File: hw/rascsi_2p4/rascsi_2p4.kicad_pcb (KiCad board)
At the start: 2 copper layers, 65 x 56 mm, 126 parts, among them J1 Raspberry_Pi_2_3, J10 Conn_01x04_Male, J2 DNP, J20 171826-4, J3 Conn_02x25_Odd_Even, J4 I2C Pinout, J5 DNP, J6 CONNFLY DB-25, J7 DNP, J8 USB_B_Micro, J9 Conn_02x25_Odd_Even, U1 74ALVC164245DGG, U2 74ALVC164245DGG, X1 Mac, X3 Mac, X7 Pi, X8 Pi

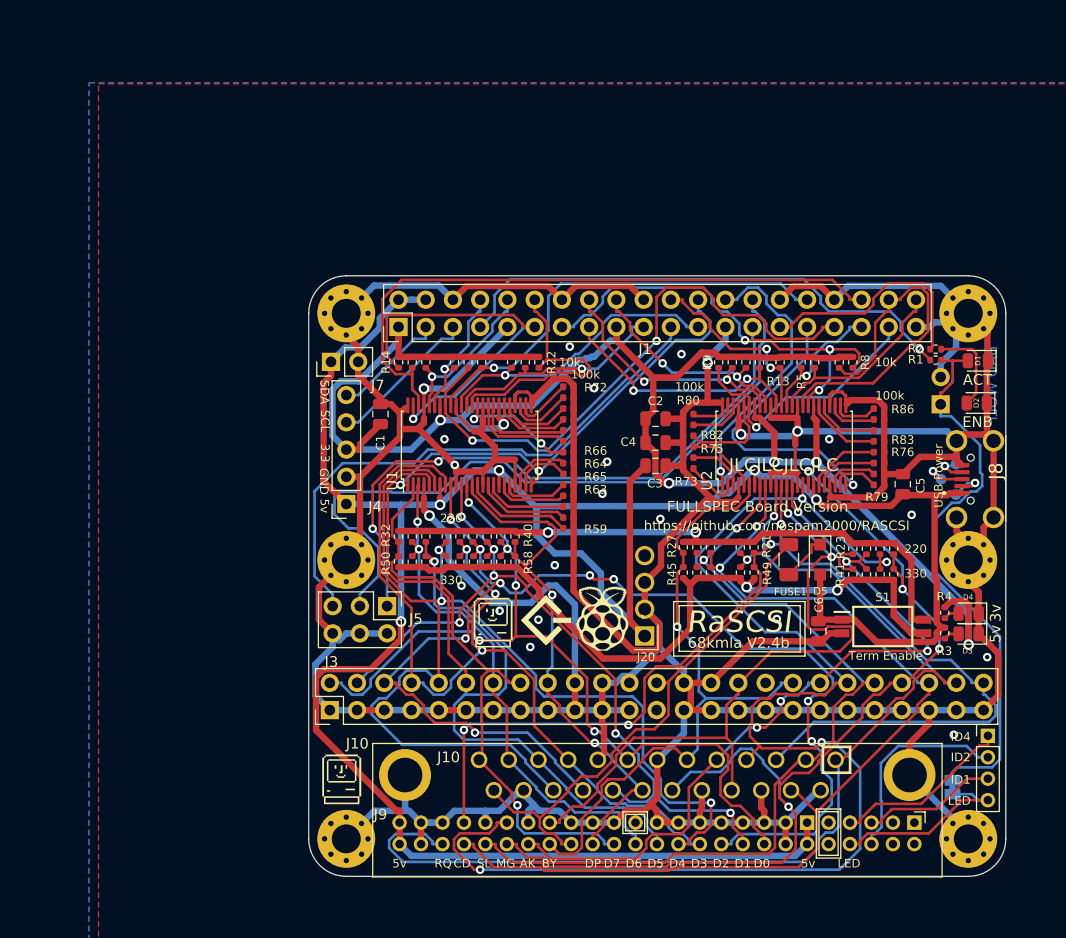
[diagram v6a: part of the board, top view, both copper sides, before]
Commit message: use active SCSI termination
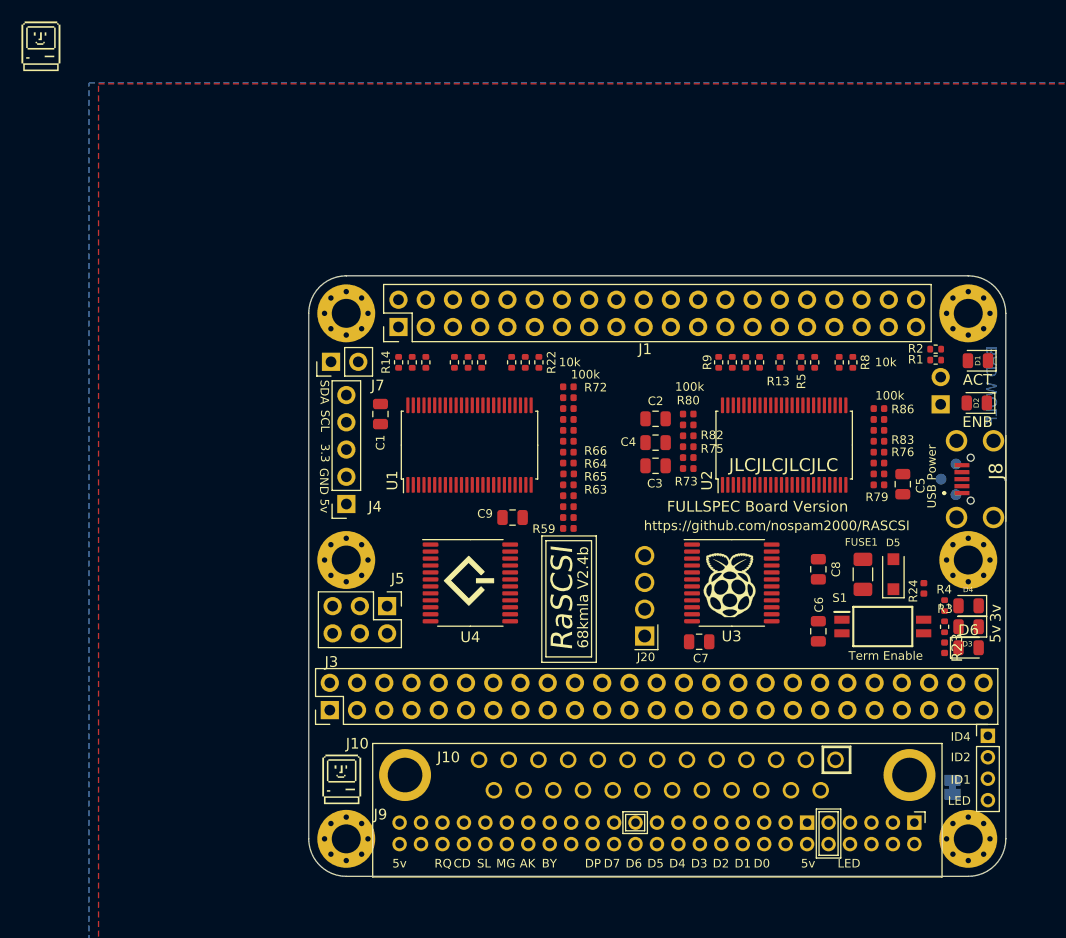
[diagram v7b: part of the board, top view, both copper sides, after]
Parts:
- removed R25, R26, R27, R28, R29, R30, R31, R32, R33, R34, R35, R36, R37, R38, R39, R40: 220, Resistor_SMD:R_0402_1005Metric
- removed R41, R42, R43, R44, R45, R46, R47, R48, R49, R50, R51, R52, R53, R54, R55, R56, R57, R58: 330, Resistor_SMD:R_0402_1005Metric
- added C7: 4u7, Capacitor_SMD:C_0805_2012Metric, F.Cu at (210.9, 76.6)
- added C8: 4u7, Capacitor_SMD:C_0805_2012Metric, F.Cu at (222.0, 69.9)
- added C9: 4u7, Capacitor_SMD:C_0805_2012Metric, F.Cu at (193.5, 65.0)
- added D6: Green, LED_SMD:LED_0805_2012Metric, F.Cu at (236.0, 77.2)
- added U3: UCC5606PWPTR, Package_SO:TSSOP-24_6.1x7.8mm_P0.65mm, F.Cu at (214.0, 71.1)
- added U4: UCC5606PWPTR, Package_SO:TSSOP-24_6.1x7.8mm_P0.65mm, F.Cu at (189.6, 71.1)
- R23: value 220 -> 2k
- R24: value 220 -> 10k
- moved X3 68.3 mm to (149.6, 21.1)
- moved R23 12.6 mm to (233.8, 77.2)
- moved X7 12.3 mm to (213.8, 71.4)
- moved X8 8.09 mm to (189.3, 70.9)
- moved FUSE1 7.04 mm to (226.2, 70.3), turned to 270 degrees
- moved D5 6.96 mm to (229.0, 70.3), turned to 90 degrees
- moved R24 6.51 mm to (231.9, 71.6), turned to 90 degrees
- moved D4 0.71 mm to (236.0, 73.3)
- moved R4 0.66 mm to (233.8, 73.3)
- moved D3 0.66 mm to (236.0, 75.2)
- moved R3 0.59 mm to (233.8, 75.2), turned to 90 degrees
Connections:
- net Net-(D5-Pad1) renamed TERMPOW_UNFUSED
- J20 pad 4: Net-(J20-Pad4) -> (no net)
- J3 pad 25: Net-(J3-Pad25) -> (no net)
- J3 pad 34: Net-(J3-Pad34) -> (no net)
- J9 pad 1: Net-(J9-Pad1) -> (no net)
- J9 pad 10: Net-(J9-Pad10) -> (no net)
- J9 pad 2: Net-(J9-Pad2) -> (no net)
- J9 pad 27: Net-(J9-Pad27) -> (no net)
- J9 pad 3: Net-(J9-Pad3) -> (no net)
- J9 pad 4: Net-(J9-Pad4) -> (no net)
- J9 pad 9: Net-(J9-Pad9) -> (no net)
- R23 pad 1: /TERM_5v -> +5V
- R23 pad 2: C-ATN -> Net-(D6-Pad2)
- R24 pad 1: /TERM_5v -> ~TERM_ENABLE
- R24 pad 2: C-ACK -> +5V
- S1 pad 1: +5V -> GND
- S1 pad 2: GND -> (no net)
- S1 pad 3: /TERM_GND -> (no net)
- S1 pad 4: /TERM_5v -> ~TERM_ENABLE
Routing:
- net GND: track 640.0 -> 0.00 mm, vias 23 -> 0
- net +5V: track 242.7 -> 0.00 mm, vias 5 -> 0
- net +3V3: track 167.3 -> 0.00 mm, vias 6 -> 0
- net C-RST: track 125.4 -> 0.00 mm, vias 4 -> 0
- net C-D2: track 115.7 -> 0.00 mm, vias 9 -> 0
- net C-D4: track 108.2 -> 0.00 mm, vias 3 -> 0
- net C-REQ: track 106.6 -> 0.00 mm, vias 2 -> 0
- net C-I_O: track 105.6 -> 0.00 mm, vias 4 -> 0
- net C-SEL: track 100.7 -> 0.00 mm, vias 4 -> 0
- net C-C_D: track 94.1 -> 0.00 mm, vias 2 -> 0
- net C-D3: track 81.7 -> 0.00 mm, vias 3 -> 0
- net C-D5: track 79.8 -> 0.00 mm, vias 1 -> 0
- net C-MSG: track 79.4 -> 0.00 mm, vias 2 -> 0
- net C-D0: track 78.1 -> 0.00 mm, vias 5 -> 0
- net C-ACK: track 73.1 -> 0.00 mm, vias 5 -> 0
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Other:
- board text removed: "220"
- board text removed: "330"

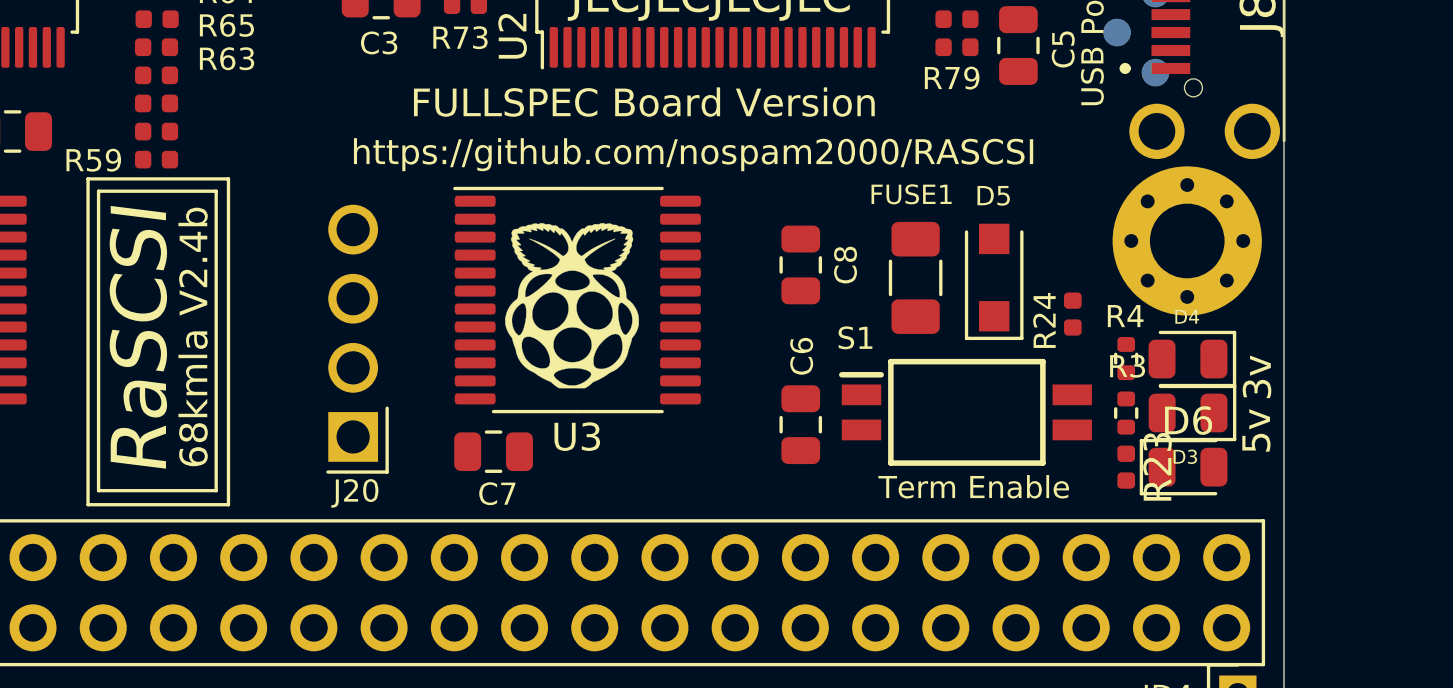
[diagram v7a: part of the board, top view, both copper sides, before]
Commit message: moved C7 and fixed some silkscreen text positions
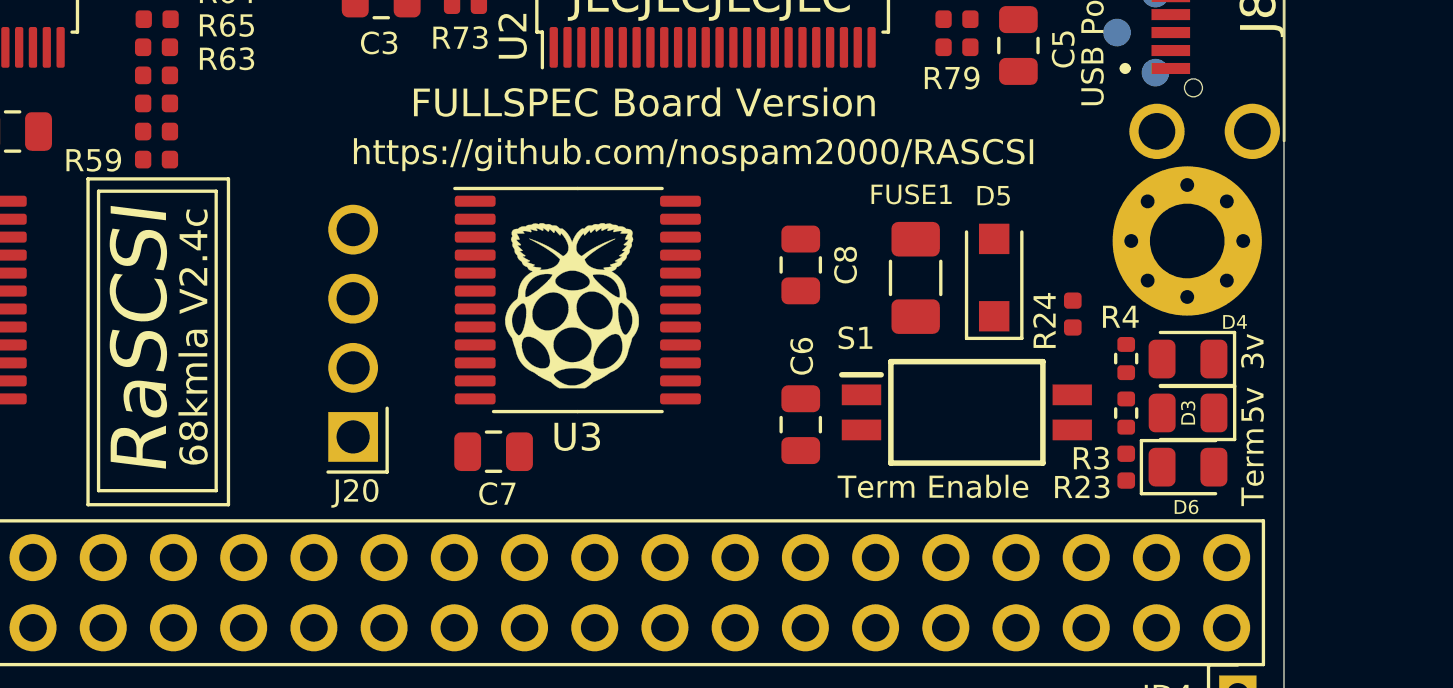
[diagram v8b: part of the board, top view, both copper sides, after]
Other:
- board text added: "68kmla V2.4c"
- board text added: "68kmla Version 2.4c"
- board text added: "Term"
- board text removed: "68kmla V2.4b"
- board text removed: "68kmla Version 2.4b"
